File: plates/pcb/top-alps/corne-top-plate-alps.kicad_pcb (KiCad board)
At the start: 2 copper layers, 132.9 x 91.4 mm, 28 parts, among them SW2 KEY_SWITCH

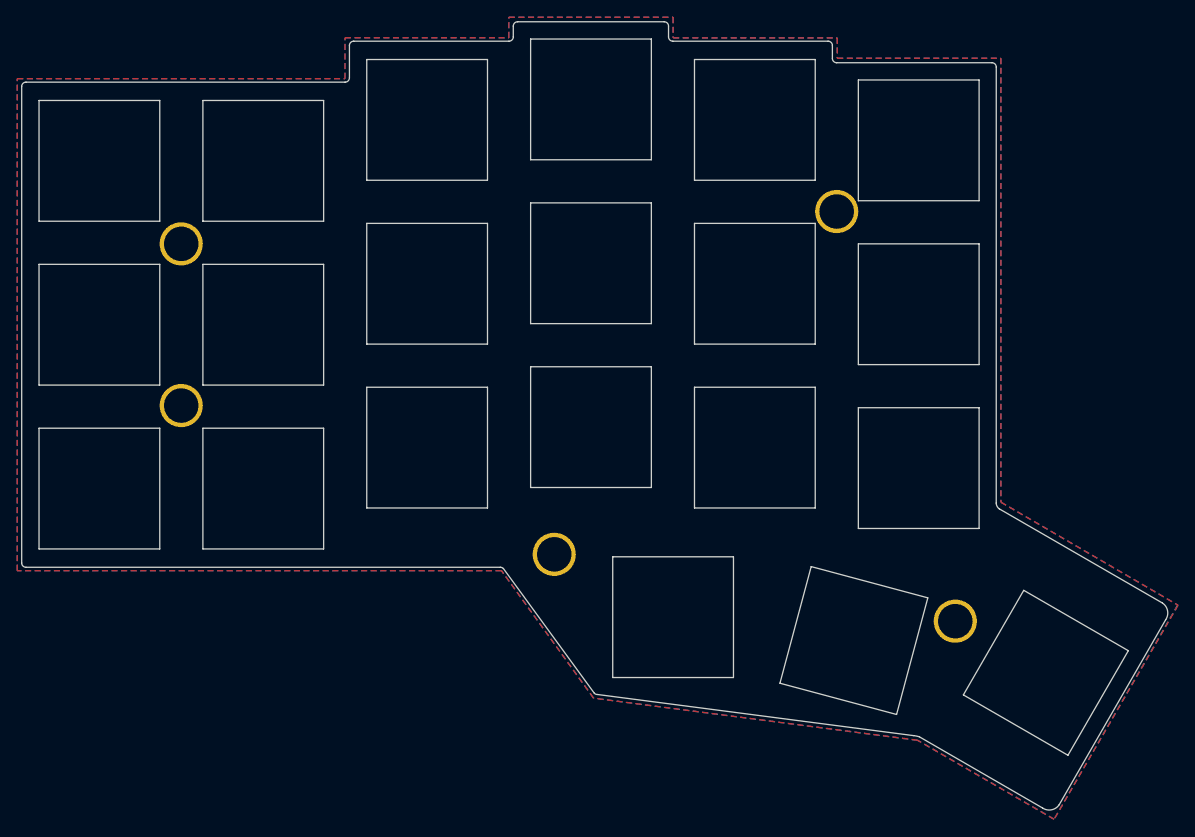
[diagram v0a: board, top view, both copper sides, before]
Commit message: Create or Update plate data for corne-light
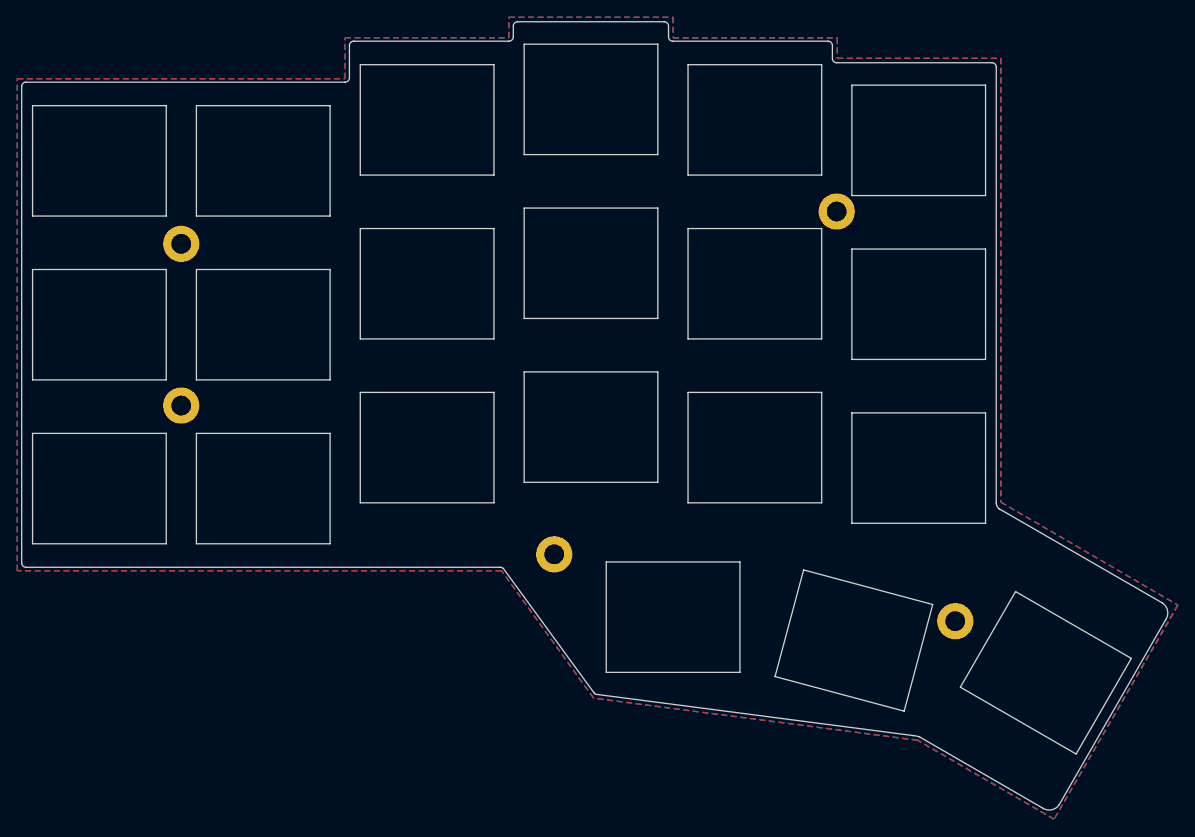
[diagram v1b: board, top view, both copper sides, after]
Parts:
- ? (x5): footprint kbd:M2_Hole_TH_Outside -> kbd:M2_Hole_TH
- SW2 (x21): footprint kbd:SW_Hole -> kbd:SW_Hole_ALPS
